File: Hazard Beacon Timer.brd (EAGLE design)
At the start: 100 x 80 mm, 20 parts

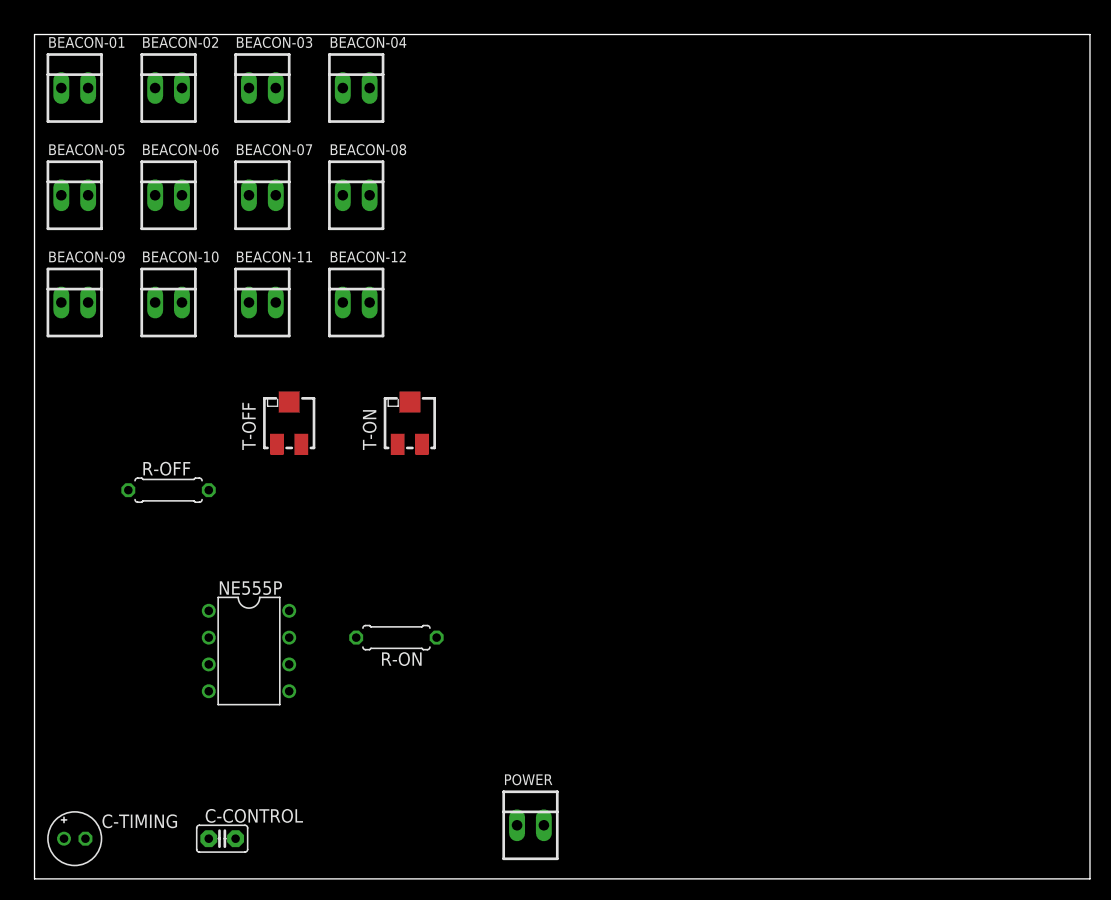
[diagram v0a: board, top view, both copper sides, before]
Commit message: Beacon Control Board update
- Rename Schematic to Hazard Beacon Timer since there are going to be other components/boards.
- Update board diagram to a more final layout.
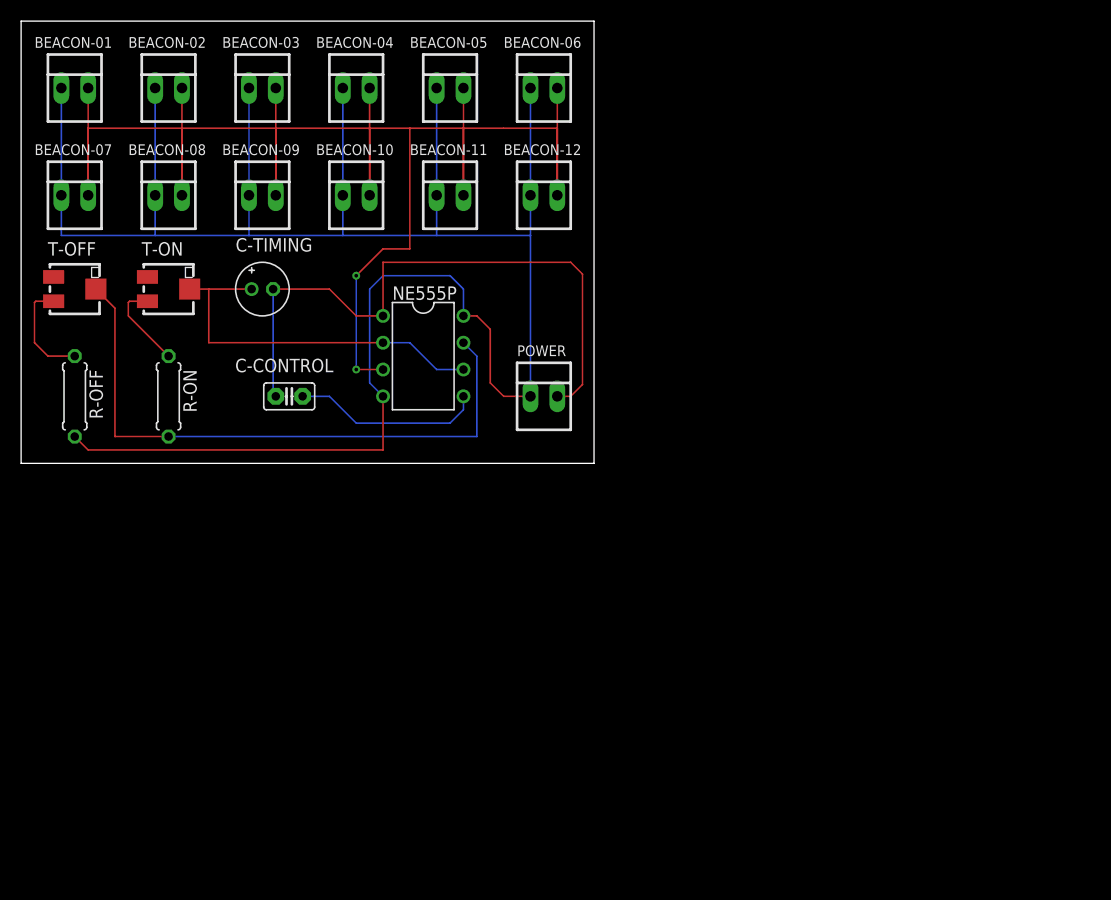
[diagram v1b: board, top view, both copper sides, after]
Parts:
- moved C-TIMING 55.0 mm to (21.6, 55.9)
- moved C-CONTROL 42.4 mm to (24.1, 45.7), turned to 180 degrees
- moved POWER 40.7 mm to (48.3, 45.7)
- moved BEACON-06 37.0 mm to (48.3, 74.9)
- moved BEACON-05 37.0 mm to (39.4, 74.9)
- moved NE555P 32.5 mm to (36.8, 49.5)
- moved R-ON 31.4 mm to (12.7, 45.7), turned to 270 degrees
- moved T-ON 26.2 mm to (12.7, 55.9), turned to 270 degrees
- moved T-OFF 24.0 mm to (3.81, 55.9), turned to 270 degrees
- moved BEACON-09 20.5 mm to (21.6, 64.8)
- moved BEACON-10 20.5 mm to (30.5, 64.8)
- moved BEACON-11 20.5 mm to (39.4, 64.8)
- moved BEACON-12 20.5 mm to (48.3, 64.8)
- moved BEACON-07 17.8 mm to (3.81, 64.8)
- moved BEACON-08 17.8 mm to (12.7, 64.8)
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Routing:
- net N$4: track 0.00 -> 214.0 mm
- net N$7: track 0.00 -> 172.5 mm, vias 0 -> 2
- net N$11: track 0.00 -> 59.5 mm
- net N$3: track 0.00 -> 58.4 mm
- net N$8: track 0.00 -> 36.1 mm
- net N$1: track 0.00 -> 18.1 mm
- net N$5: track 0.00 -> 10.0 mm
- net N$2: track 0.00 -> 8.52 mm
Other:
- board size 100 x 80 mm -> 54.3 x 41.9 mm
